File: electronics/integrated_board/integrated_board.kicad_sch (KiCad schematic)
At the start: 54 parts, among them CON1 BARREL_JACK, J1 Conn_01x04_Female, J13 Conn_01x05_Female, J15 Conn_01x05_Female, J17 Conn_01x05_Female, P10 Conn_01x02, P15 Conn_01x02, P16 UART, P2 A1, P3 A2, P4 A3, P5 I2C 2, U3 LM2596T-5, U4 ESP32-DEVKITC-32D, U5 ULN2003, U6 ULN2003

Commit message: update integrated board
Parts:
- removed C1 (x3), C2 (x3): 22nF, Capacitor_THT:CP_Radial_D4.0mm_P2.00mm, symbol Device:C
- removed C7, C8: C_Small, Capacitor_THT:C_Disc_D6.0mm_W4.4mm_P5.00mm, symbol Device:C_Small
- removed J1 (x3): Conn_01x04_Female, Connector_JST:JST_XH_B4B-XH-A_1x04_P2.50mm_Vertical, symbol Connector:Conn_01x04_Female
- removed P5: I2C 2, Connector_JST:JST_XH_B4B-XH-A_1x04_P2.50mm_Vertical, symbol Connector_Generic:Conn_01x04
- removed R1 (x3), R3 (x3), R5 (x3), R6 (x3): 1k, Resistor_THT:R_Axial_DIN0309_L9.0mm_D3.2mm_P12.70mm_Horizontal, symbol Device:R
- removed R2 (x3), R4 (x3): 1.8k, Resistor_THT:R_Axial_DIN0309_L9.0mm_D3.2mm_P12.70mm_Horizontal, symbol Device:R
- removed U5, U6: ULN2003, Package_DIP:DIP-16_W7.62mm_Socket_LongPads, symbol Transistor_Array:ULN2003
- added C1, C13, C2, C7, C8, C9: 22nF, Capacitor_THT:CP_Radial_D4.0mm_P2.00mm, symbol Device:C
- added C3, C4: C_Small, Capacitor_THT:C_Disc_D6.0mm_W4.4mm_P5.00mm, symbol Device:C_Small
- added J1: to_rotary_encoder3(12,13), Connector_JST:JST_XH_B4B-XH-A_1x04_P2.50mm_Vertical, symbol Connector:Conn_01x04_Female
- added J2: to_rotary_encoder3, Connector_JST:JST_XH_B4B-XH-A_1x04_P2.50mm_Vertical, symbol Connector:Conn_01x04_Female
- added J5: to_rotary_encoder2 (14,27), Connector_JST:JST_XH_B4B-XH-A_1x04_P2.50mm_Vertical, symbol Connector:Conn_01x04_Female
- added P1: Conn_01x02, Connector_JST:JST_XH_B2B-XH-A_1x02_P2.50mm_Vertical, symbol Connector_Generic:Conn_01x02
- added P6: io, Connector_JST:JST_XH_B4B-XH-A_1x04_P2.50mm_Vertical, symbol Connector_Generic:Conn_01x04
- added Q1, Q2, Q3, Q4, Q5, Q6: 2N7000, Package_TO_SOT_THT:TO-92_Inline_Wide, symbol Transistor_FET:2N7000
- added R1, R10, R11, R12, R13, R2, R29, R3, R30, R4, R8, R9: 1k, Resistor_THT:R_Axial_DIN0411_L9.9mm_D3.6mm_P12.70mm_Horizontal, symbol Device:R
- added R14, R15, R28, R31, R5, R6: 1k, Resistor_THT:R_Axial_DIN0309_L9.0mm_D3.2mm_P12.70mm_Horizontal, symbol Device:R
- added U1, U2: ULN2003, Package_DIP:DIP-16_W7.62mm_LongPads, symbol Transistor_Array:ULN2003
- J13: value Conn_01x05_Female -> to_motor1(2,15,16,17)
- J15: value Conn_01x05_Female -> to_motor2 (5,18,19,21)
- J17: value Conn_01x05_Female -> to_motor3 (22,23,9,10)
- P2: value A1 -> io
- P4: value A3 -> io
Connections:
- net +5V: now also C3.2, C4.2, J1.3 (Pin_3), J2.3 (Pin_3), J5.3 (Pin_3), P6.3 (Pin_3), R12.1, R13.1, R14.2, R15.1, R28.2, R29.1, R3.1, R31.1, R4.1, R5.2, R6.1, R9.1, U1.9 (COM), U2.9 (COM)
- net GND: now also C1.2, C13.2, C2.2, C3.1, C4.1, C7.2, C8.2, C9.2, J1.4 (Pin_4), J2.4 (Pin_4), J5.4 (Pin_4), P6.4 (Pin_4), U1.8 (GND), U2.8 (GND)
- net at J15.1 (Pin_1): now also U2.14 (O3)
- net at J15.2 (Pin_2): now also U2.15 (O2)
- net at J15.3 (Pin_3): now also U2.16 (O1)
- net at J15.4 (Pin_4): now also U1.10 (O7)
- net at J13.1 (Pin_1): now also U2.10 (O7)
- net at J13.2 (Pin_2): now also U2.11 (O6)
- net at J13.3 (Pin_3): now also U2.12 (O5)
- net at J13.4 (Pin_4): now also U2.13 (O4)
- net at C5.1, P10.1 (Pin_1), P15.1 (Pin_1)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: now also P1.2 (Pin_2); no longer CON1.1
- net at J17.1 (Pin_1): now also U1.11 (O6)
- net at J17.2 (Pin_2): now also U1.12 (O5)
- net at J17.3 (Pin_3): now also U1.13 (O4)
- net at J17.4 (Pin_4): now also U1.14 (O3)
- net +3V3: now reaches U4.1 (3V3)
- net +3V3: now also Q1.2 (G), Q2.2 (G), Q3.2 (G), Q4.2 (G), Q5.2 (G), Q6.2 (G), R1.1, R10.1, R11.1, R2.1, R30.1, R8.1
- net A1-3: no longer names the net of P2.1 (Pin_1)
- net A1-3: now also U4.8 (IO33); no longer U4.6 (IO35)
- net A1-4: no longer names the net of P2.2 (Pin_2)
- net A1-4: now also U4.7 (IO32); no longer U4.5 (IO34)
- net A3-3: no longer names the net of P4.1 (Pin_1)
- net A3-3: now also U4.6 (IO35); no longer U4.7 (IO32)
- net A3-4: no longer names the net of P4.2 (Pin_2)
- net A3-4: now also U4.5 (IO34); no longer U4.8 (IO33)
- net D1-3: no longer names the net of U4.35 (IO15)
- net D1-3: now also U2.7 (I7)
- net D1-4: no longer names the net of U4.34 (IO2)
- net D1-4: now also U2.6 (I6)
- net D2-3: no longer names the net of U4.33 (IO0)
- net D2-3: now also P6.2 (Pin_2)
- net D2-4: no longer names the net of U4.32 (IO4)
- net D2-4: now also P6.1 (Pin_1)
- net D3-3: no longer names the net of U4.31 (IO16)
- net D3-3: now also U2.5 (I5)
- net D3-4: no longer names the net of U4.30 (IO17)
- net D3-4: now also U2.4 (I4)
- net D4-3: no longer names the net of U4.29 (IO5)
- net D4-3: now also U2.3 (I3)
- net D4-4: no longer names the net of U4.28 (IO18)
- net D4-4: now also U2.2 (I2)
- net D5-3: no longer names the net of U4.27 (IO19)
- net D5-3: now also U2.1 (I1)
- net D5-4: no longer names the net of U4.25 (IO21)
- net D5-4: now also U1.7 (I7)
- net D6-3: no longer names the net of U4.22 (IO22)
- net D6-3: now also U1.6 (I6)
- net D6-4: no longer names the net of U4.21 (IO23)
- net D6-4: now also U1.5 (I5)
- net D7-3: no longer names the net of U4.12 (IO14)
- net D7-3: now also Q6.1 (S), R8.2
- net D7-4: no longer names the net of U4.11 (IO27)
- net D7-4: now also Q5.1 (S), R30.2
- net D8-3: no longer names the net of U4.10 (IO26)
- net D8-3: now also Q4.1 (S), R11.2
- net D8-4: no longer names the net of U4.9 (IO25)
- net D8-4: now also Q3.1 (S), R10.2
- net I2C_1-3 renamed to_uln2003_2
- net to_uln2003_2: now also U1.3 (I3)
- net I2C_1-4 renamed to_uln2003_1
- net to_uln2003_1: now also U1.4 (I4)
- net I2C_2-3: no longer names the net of U4.13 (IO12)
- net I2C_2-3: now also Q2.1 (S), R2.2
- net I2C_2-4: no longer names the net of U4.15 (IO13)
- net I2C_2-4: now also Q1.1 (S), R1.2
- new net: C2.1, J1.1 (Pin_1), Q2.3 (D), R4.2, R6.2
- new net: C1.1, J1.2 (Pin_2), Q1.3 (D), R3.2, R5.1
- new net: C8.1, J2.1 (Pin_1), Q3.3 (D), R12.2, R14.1
- new net: C9.1, J2.2 (Pin_2), Q4.3 (D), R13.2, R15.2
- new net: C7.1, J5.2 (Pin_2), Q6.3 (D), R31.2, R9.2
- new net: C13.1, J5.1 (Pin_1), Q5.3 (D), R28.1, R29.2
- new net: CON1.1, P1.1 (Pin_1)
- no-connect marks 10 -> 9
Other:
- note removed: "1 2 3 4"
- note removed: "Connector pinin"
- note removed: "I2C"
- note removed: "channel A channel B vcc gnd"
- moved on the sheet: C5, C6, CON1, D1, D2, J13, J15, J17, L1, P10, P15, P3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

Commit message: update integrated board
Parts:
- removed P3: A2, Connector_JST:JST_XH_B4B-XH-A_1x04_P2.50mm_Vertical, symbol Connector_Generic:Conn_01x04
- removed P6: io, Connector_JST:JST_XH_B4B-XH-A_1x04_P2.50mm_Vertical, symbol Connector_Generic:Conn_01x04
- added R16, R17: 10k, Resistor_THT:R_Axial_DIN0411_L9.9mm_D3.6mm_P12.70mm_Horizontal, symbol Device:R
- added R18, R19, R20, R21: 1k, Resistor_THT:R_Axial_DIN0411_L9.9mm_D3.6mm_P12.70mm_Horizontal, symbol Device:R
- added SW1, SW2: SW_Push, Connector_JST:JST_XH_B2B-XH-A_1x02_P2.50mm_Vertical, symbol Switch:SW_Push
- J13: value to_motor1(2,15,16,17) -> to_motor1(15,2,0,4)
- J15: value to_motor2 (5,18,19,21) -> to_motor2 (16,17,5,18)
- J17: value to_motor3 (22,23,9,10) -> to_motor3 (19,21,22,23)
- P2: value io -> LCD
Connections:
- net +5V: now also R18.1
- net GND: now also R16.2, R17.1, R19.1
- net encoderY_1: now reaches Q3.1 (S), R10.2
- net encoderY_1: now also U4.10 (IO26); no longer U4.9 (IO25)
- net encoderZ_1: now reaches Q1.1 (S), R1.2
- net encoderZ_1: now also U4.6 (IO35); no longer U4.15 (IO13)
- net encoderX_1: now reaches Q6.1 (S), R8.2, U4.12 (IO14)
- net at U2.1 (I1): now also U4.29 (IO5); no longer U4.27 (IO19)
- net at U2.2 (I2): now also U4.30 (IO17); no longer U4.28 (IO18)
- net at U2.3 (I3): now also U4.31 (IO16); no longer U4.29 (IO5)
- net at U2.4 (I4): now also U4.32 (IO4); no longer U4.30 (IO17)
- net at U2.5 (I5): now also U4.33 (IO0); no longer U4.31 (IO16)
- net encoderY_2: now reaches Q4.1 (S), R11.2
- net encoderY_2: now also U4.9 (IO25); no longer U4.10 (IO26)
- net encoderX_2: now reaches Q5.1 (S), R30.2, U4.11 (IO27)
- net at U4.21 (IO23): now also U1.3 (I3); no longer U1.5 (I5)
- net at U4.22 (IO22): now also U1.4 (I4); no longer U1.6 (I6)
- net at U4.25 (IO21): now also U1.5 (I5); no longer U1.7 (I7)
- net at P4.1 (Pin_1): now also U4.15 (IO13); no longer U4.6 (IO35)
- net at P4.2 (Pin_2): now also U4.13 (IO12); no longer U4.5 (IO34)
- net encoderZ_2: now reaches Q2.1 (S), R2.2
- net encoderZ_2: now also U4.5 (IO34); no longer U4.13 (IO12)
- net A2-3 renamed switch1
- net switch1: now also R16.1, SW1.1
- net A2-4 renamed switch2
- net switch2: now also R17.2, SW2.1
- net to_uln2003_1: no longer names the net of U4.17 (SD3)
- net to_uln2003_1: no longer U1.4 (I4)
- net to_uln2003_2: no longer names the net of U4.16 (SD2)
- net to_uln2003_2: no longer U1.3 (I3)
- new net: R18.2, R19.2, R20.2, R21.2
- new net: R20.1, SW1.2
- new net: U1.6 (I6), U4.27 (IO19)
- new net: U1.7 (I7), U4.28 (IO18)
- new net: R21.1, SW2.2
- no-connect marks 9 -> 11
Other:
- note removed: "Analog"
- moved on the sheet: C1, C13, C2, C3, C4, C5, C6, C7, C8, C9, CON1, D1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

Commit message: finish revision of integrated pcb board, create production files
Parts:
- removed C13, C7: 22nF, Capacitor_THT:CP_Radial_D4.0mm_P2.00mm, symbol Device:C
- removed J5: to_rotary_encoder2 (14,27), Connector_JST:JST_XH_B4B-XH-A_1x04_P2.50mm_Vertical, symbol Connector:Conn_01x04_Female
- removed Q1, Q2, Q3, Q4, Q5, Q6: 2N7000, Package_TO_SOT_THT:TO-92_Inline_Wide, symbol Transistor_FET:2N7000
- removed R28, R31: 1k, Resistor_THT:R_Axial_DIN0309_L9.0mm_D3.2mm_P12.70mm_Horizontal, symbol Device:R
- removed R29, R30, R8, R9: 1k, Resistor_THT:R_Axial_DIN0411_L9.9mm_D3.6mm_P12.70mm_Horizontal, symbol Device:R
- added C10, C11: 22nF, Capacitor_THT:C_Disc_D6.0mm_W4.4mm_P5.00mm, symbol Device:C
- added J3: to_rotary_encoderX(14,27), Connector_JST:JST_XH_B4B-XH-A_1x04_P2.50mm_Vertical, symbol Connector:Conn_01x04_Female
- added R22, R23, R25, R26: 1kΩ, Resistor_THT:R_Axial_DIN0309_L9.0mm_D3.2mm_P12.70mm_Horizontal, symbol Device:R
- added R24, R27: 1.8k, Resistor_THT:R_Axial_DIN0309_L9.0mm_D3.2mm_P12.70mm_Horizontal, symbol Device:R
- C1, C2, C8, C9: footprint Capacitor_THT:CP_Radial_D4.0mm_P2.00mm -> Capacitor_THT:C_Disc_D6.0mm_W4.4mm_P5.00mm
- J1: value to_rotary_encoder3(12,13) -> to_rotary_encoderZ(35,34)
- J2: value to_rotary_encoder3 -> to_rotary_encoderY(25,26)
- R1, R10, R11, R13, R2, R4: value 1k -> 1kΩ; footprint Resistor_THT:R_Axial_DIN0411_L9.9mm_D3.6mm_P12.70mm_Horizontal -> Resistor_THT:R_Axial_DIN0309_L9.0mm_D3.2mm_P12.70mm_Horizontal
- R12, R3: value 1k -> 1.8k; footprint Resistor_THT:R_Axial_DIN0411_L9.9mm_D3.6mm_P12.70mm_Horizontal -> Resistor_THT:R_Axial_DIN0309_L9.0mm_D3.2mm_P12.70mm_Horizontal
- R14, R5: value 1k -> 1kΩ
- R15, R6: value 1k -> 1.8k
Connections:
- net +3V3: no longer R1.1, R10.1, R11.1, R2.1
- net +5V: now also R1.2, R10.2, R13.2, R4.2, J3.3 (Pin_3), R22.2, R25.2; no longer R12.1, R13.1, R14.2, R15.1, R3.1, R4.1, R5.2, R6.1
- net GND: now also C1.1, C2.1, C8.1, C9.1, R12.1, R15.1, R3.1, R6.1, C10.1, C11.1, J3.4 (Pin_4), R24.1, R27.1; no longer C1.2, C2.2, C8.2, C9.2
- net encoderX_1: now also R14.1, R15.2
- net encoderX_2: now also R11.1, R12.2
- net encoderY_1: now also R2.1, R3.2; no longer R10.2
- net encoderY_2: now also R5.1, R6.2; no longer R11.2
- net encoderZ_1: now also R23.1, R24.2; no longer R1.2
- net encoderZ_2: now also R26.1, R27.2; no longer R2.2
- new net: C10.2, J1.1 (Pin_1), R22.1, R23.2
- new net: C11.2, J1.2 (Pin_2), R25.1, R26.2
- new net: C8.2, J3.1 (Pin_1), R10.1, R11.2
- new net: C2.2, J2.2 (Pin_2), R4.1, R5.2
- new net: C9.2, J3.2 (Pin_2), R13.1, R14.2
- new net: C1.2, J2.1 (Pin_1), R1.1, R2.2
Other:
- moved on the sheet: J1, J2

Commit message: fix board bugs
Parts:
- removed R20, R21: 1k, Resistor_THT:R_Axial_DIN0411_L9.9mm_D3.6mm_P12.70mm_Horizontal, symbol Device:R
- C3, C4: value C_Small -> 10µF
- J1: value to_rotary_encoderZ(35,34) -> rot_encoderZ(35,34)
- J13: value to_motor1(15,2,0,4) -> motor1(15,2,0,4)
- J15: value to_motor2 (16,17,5,18) -> motor2 (16,17,5,18)
- J17: value to_motor3 (19,21,22,23) -> motor3 (19,21,22,23)
- J2: value to_rotary_encoderY(25,26) -> rot_encoderY(25,26)
- J3: value to_rotary_encoderX(14,27) -> rot_encoderX(14,27)
- R16, R17: value 10k -> 1.8k
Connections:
- net at R18.2, R19.2: now also SW1.2, SW2.2
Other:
- moved on the sheet: R13

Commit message: Expanding integrated board
-Board now incorporates pcr8575 gpio expander
-removed UART port
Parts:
- removed P4: io, Connector_JST:JST_XH_B4B-XH-A_1x04_P2.50mm_Vertical, symbol Connector_Generic:Conn_01x04
- removed R16, R17: 1.8k, Resistor_THT:R_Axial_DIN0411_L9.9mm_D3.6mm_P12.70mm_Horizontal, symbol Device:R
- removed R18, R19: 1k, Resistor_THT:R_Axial_DIN0411_L9.9mm_D3.6mm_P12.70mm_Horizontal, symbol Device:R
- removed SW1, SW2: SW_Push, Connector_JST:JST_XH_B2B-XH-A_1x02_P2.50mm_Vertical, symbol Switch:SW_Push
- added C12, C13, C14, C15, C7: C, Capacitor_THT:C_Disc_D6.0mm_W4.4mm_P5.00mm, symbol Device:C
- added J10: pcf8575 IO expander, Connector_PinHeader_2.54mm:PinHeader_1x05_P2.54mm_Vertical, symbol Connector_Generic:Conn_01x05
- added J11: Switch 1, Connector_JST:JST_XH_B2B-XH-A_1x02_P2.50mm_Vertical, symbol Connector_Generic:Conn_01x02
- added J4: Switch 2, Connector_JST:JST_XH_B2B-XH-A_1x02_P2.50mm_Vertical, symbol Connector_Generic:Conn_01x02
- added J5: Endstop A, Connector_JST:JST_XH_S2B-XH-A_1x02_P2.50mm_Horizontal, symbol Connector_Generic:Conn_01x02
- added J6: Endstop B, Connector_JST:JST_XH_S2B-XH-A_1x02_P2.50mm_Horizontal, symbol Connector_Generic:Conn_01x02
- added J7: Endstop C, Connector_JST:JST_XH_S2B-XH-A_1x02_P2.50mm_Horizontal, symbol Connector_Generic:Conn_01x02
- added J8, J9: Conn_01x16, Connector_PinHeader_2.54mm:PinHeader_1x08_P2.54mm_Vertical, symbol Connector_Generic:Conn_01x08
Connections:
- net +5V: now also J10.2 (Pin_2), J8.7 (Pin_7), J9.2 (Pin_2)
- net GND: now also C12.1, C13.1, C14.1, C15.1, C7.1, J10.1 (Pin_1), J11.1 (Pin_1), J4.1 (Pin_1), J5.1 (Pin_1), J6.1 (Pin_1), J7.1 (Pin_1), J8.8 (Pin_8), J9.1 (Pin_1)
- net at P2.1 (Pin_1), U4.8 (IO33): now also J10.4 (Pin_4)
- net at P2.2 (Pin_2), U4.7 (IO32): now also J10.3 (Pin_3)
- net at U4.15 (IO13): now also J10.5 (Pin_5)
- new net: C7.2, J5.2 (Pin_2), J9.8 (Pin_8)
- new net: C12.2, J6.2 (Pin_2), J9.7 (Pin_7)
- new net: C14.2, J4.2 (Pin_2), J8.2 (Pin_2)
- new net: C15.2, J11.2 (Pin_2), J8.1 (Pin_1)
- new net: C13.2, J7.2 (Pin_2), J9.6 (Pin_6)
- no-connect marks 11 -> 16
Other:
- moved on the sheet: C3, C4, C5, C6, CON1, D1, D2, J13, J15, J17, L1, P1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

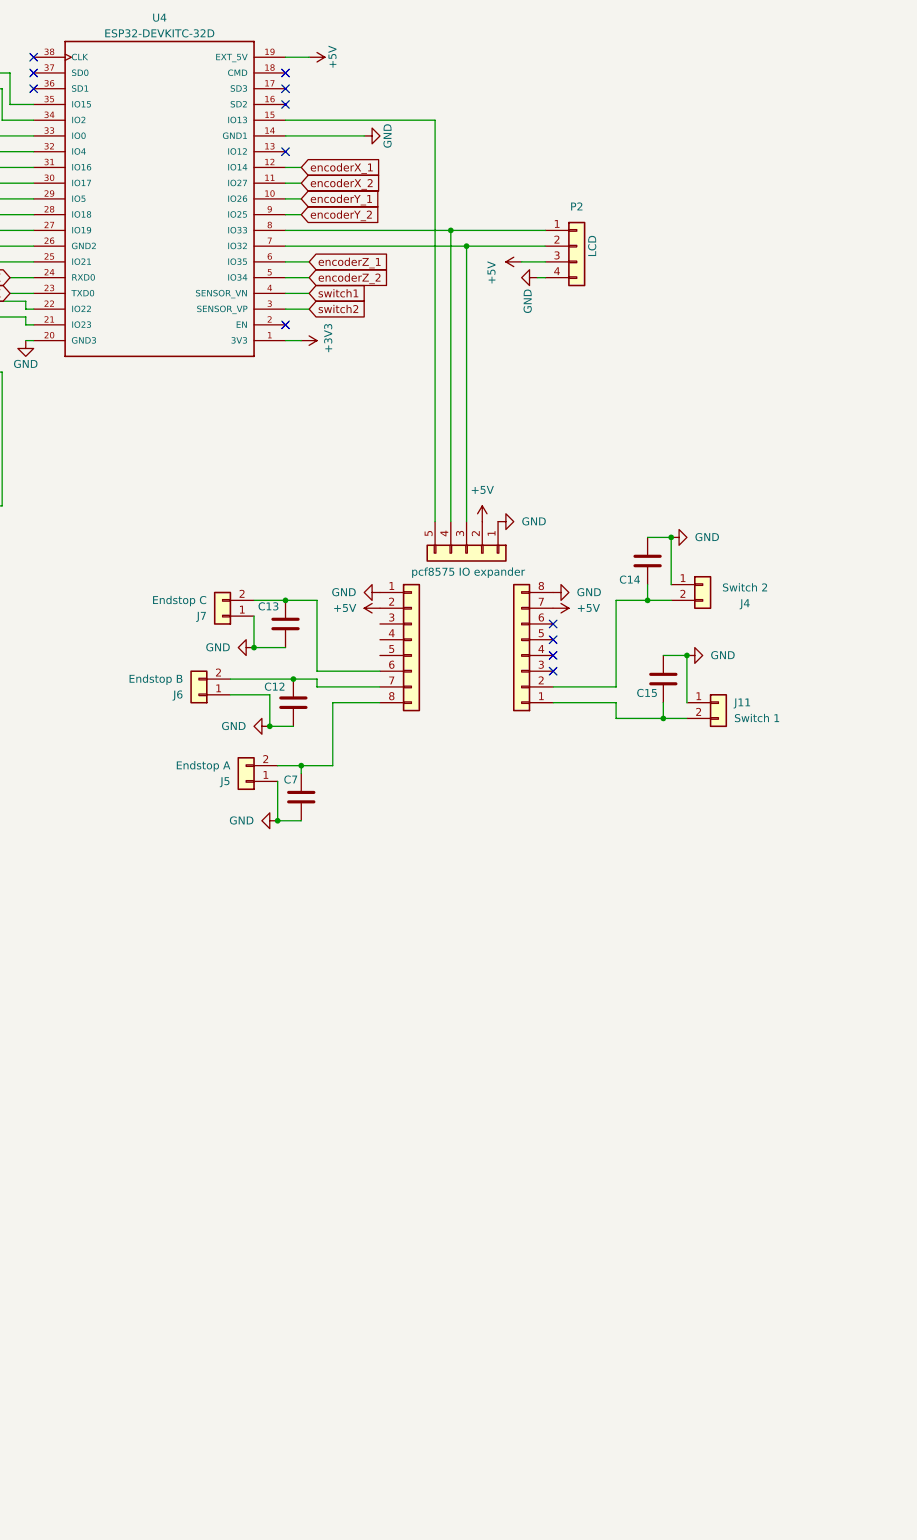
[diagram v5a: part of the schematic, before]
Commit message: Update PCB
reintroduced push-switches as controlled by individual pins for better use of interrupts
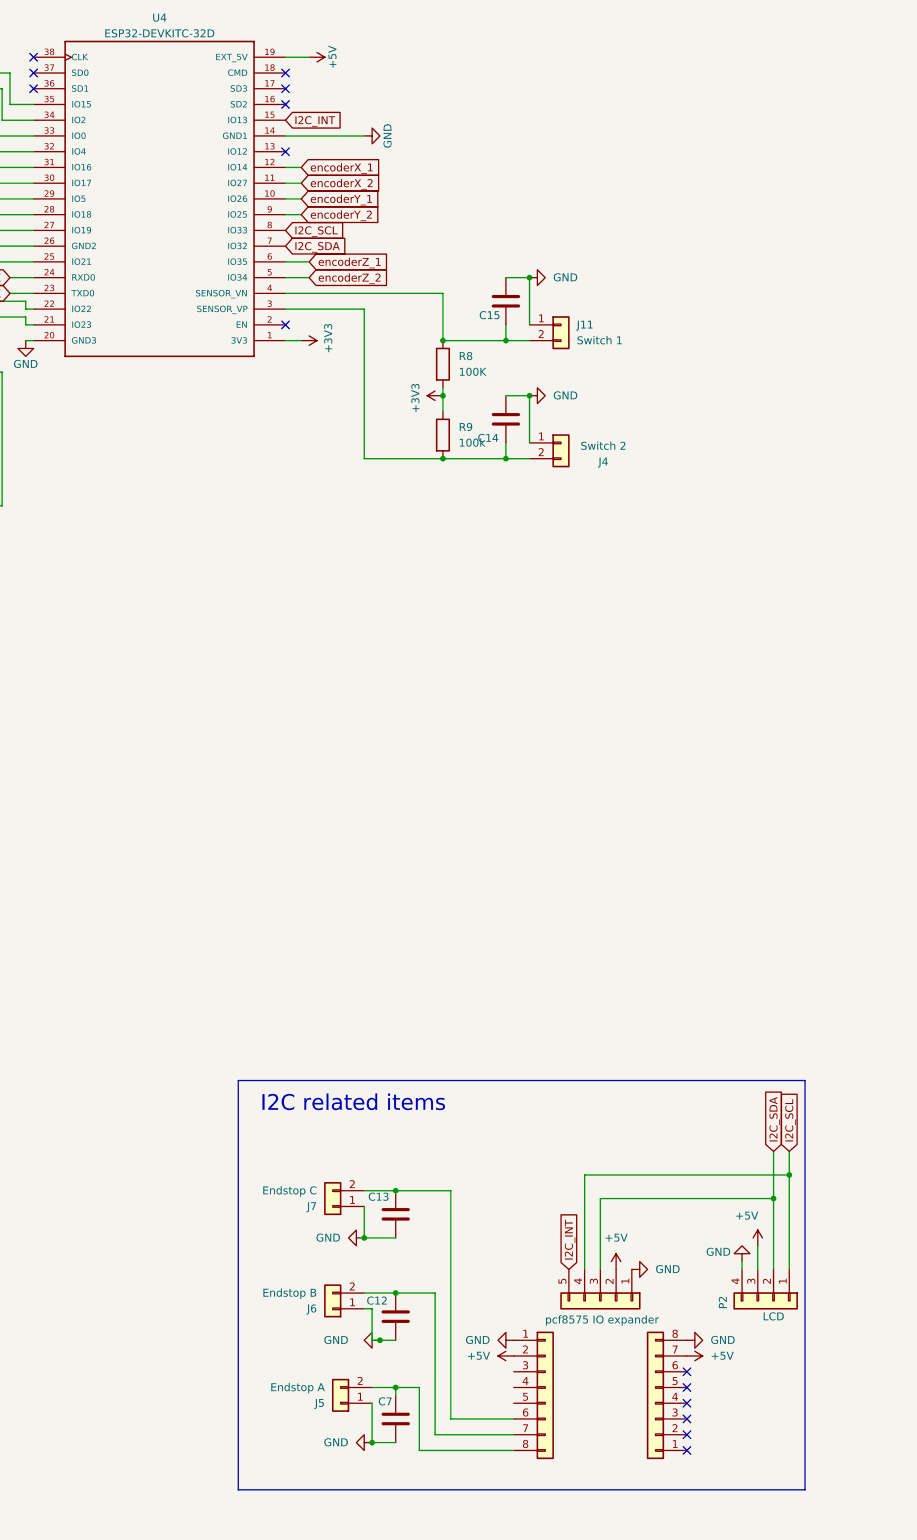
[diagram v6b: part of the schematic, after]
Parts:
- added R8: 100K, Resistor_THT:R_Axial_DIN0309_L9.0mm_D3.2mm_P12.70mm_Horizontal, symbol Device:R
- added R9: 100k, Resistor_THT:R_Axial_DIN0309_L9.0mm_D3.2mm_P12.70mm_Horizontal, symbol Device:R
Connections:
- net switch1 is gone; now on an unnamed net: U4.4 (SENSOR_VN)
- net switch2 is gone; now on an unnamed net: U4.3 (SENSOR_VP)
- net +3V3: now also R8.2, R9.1
- net at C14.2, J4.2 (Pin_2): now also R9.2; no longer J8.2 (Pin_2)
- net I2C_SDA: now reaches J10.3 (Pin_3), P2.2 (Pin_2), U4.7 (IO32)
- net I2C_SCL: now reaches J10.4 (Pin_4), P2.1 (Pin_1), U4.8 (IO33)
- net I2C_INT: now reaches J10.5 (Pin_5), U4.15 (IO13)
- net at C15.2, J11.2 (Pin_2): now also R8.1; no longer J8.1 (Pin_1)
- no-connect marks 16 -> 18
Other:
- note added: "I2C related items"
- moved on the sheet: C12, C13, C14, C15, C7, J11, J4, J5, J6, J7, P2
